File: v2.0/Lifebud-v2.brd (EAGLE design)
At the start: 100 x 80 mm, 47 parts, among them IC1 MCP73831/OT, Q1 BSS138, Q2 BSS138, Q3 BSS138, U2 MIC5219 3.3V, U3 MMA8452Q, U4 FT232RL, Y1 32.768kHz

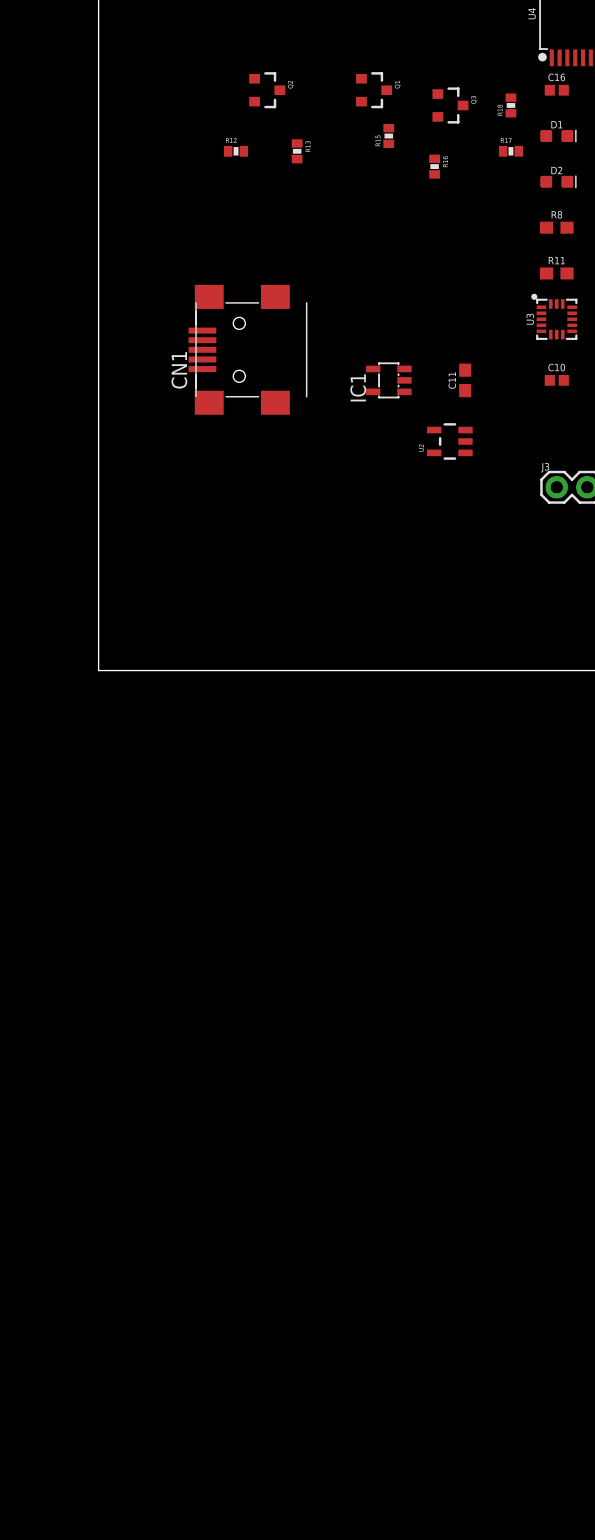
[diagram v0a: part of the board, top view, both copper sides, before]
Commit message: nearly finished with the DC/DC converter setup on nrf51
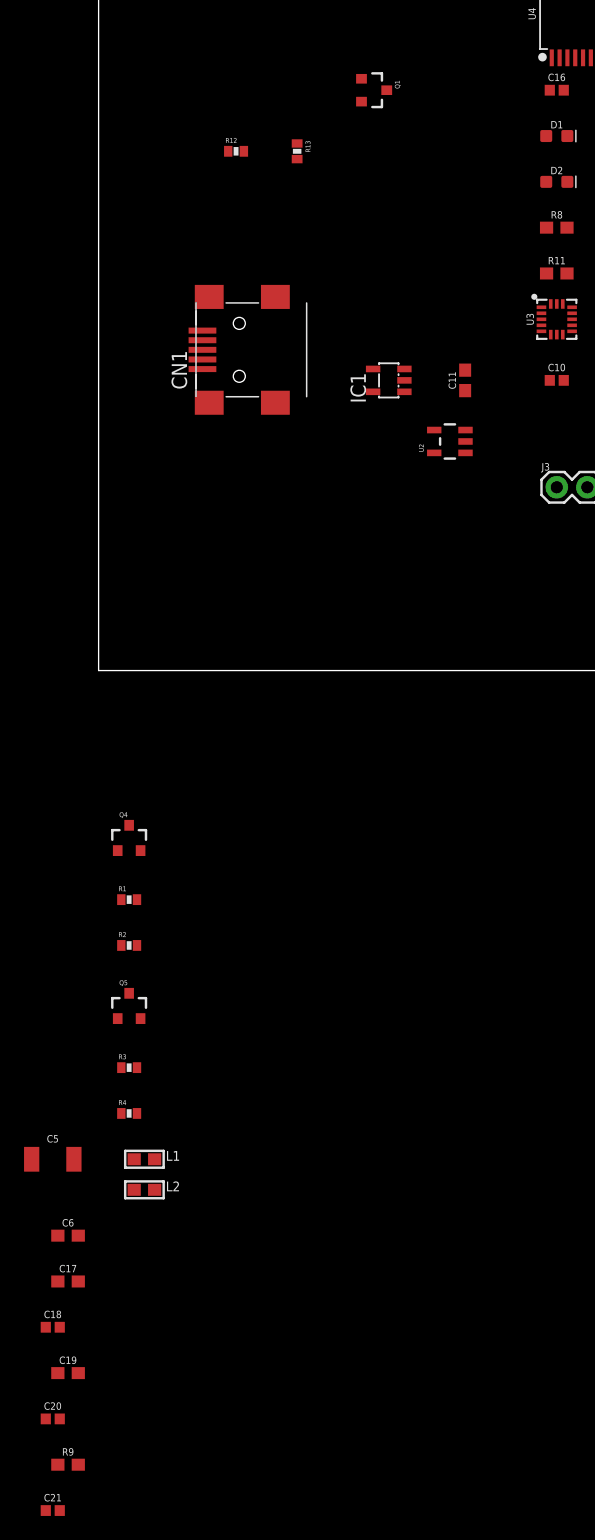
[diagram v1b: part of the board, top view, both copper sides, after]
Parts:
- removed Q2, Q3: BSS138, SparkFun:SOT23-3
- removed R15, R16, R17, R18: 10K, SparkFun:0402-RES
- added C17, C6: 1.0uF, SparkFun-Capacitors:0603
- added C18, C20, C21: 0.1uF, SparkFun-Capacitors:0402
- added C19: 4.7uF, SparkFun-Capacitors:0603
- added C5: 22UF, SparkFun-Capacitors:1210
- added L1: 10nH, microbuilder:0603
- added L2: 15nH, microbuilder:0603
- added Q4, Q5: BSS138, SparkFun:SOT23-3
- added R1, R2, R3, R4: 10K, SparkFun:0402-RES
- added R9: 10k, SparkFun-Resistors:0603
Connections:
- net N$17 renamed MAX_INT
- removed net N$18: J3.4
- removed net N$19: J3.3
- new net AVDD: C17.2, C6.1, L2.1
- new net MMA_I1: J3.4, U3.9
- new net MMA_I2: J3.3, U3.11
- new net N$20: L1.1, L2.2
- new net N$22: L1.2, U$2.15
- new net N$24: C18.2, U3.2
- new net N$25: R9.2, U3.7
- net +3V3: now also Q4.1, Q5.1, R1.1, R3.1; no longer Q2.1, Q3.1, R15.1, R17.1
- net 3V3: no longer U$1.A3
- net GND: now also C17.1, C18.1, C19.1, C20.1, C21.2, C5.1, C6.2, U3.10, U3.12, U3.5
- net INT_IN: now also Q5.3, R4.2; no longer Q3.3, R18.2
- net INT_OUT: now also Q5.2, R3.2; no longer Q3.2, R17.2
- net SCL_OUT: now also U3.4
- net SDA_IN: now also Q4.3, R2.2; no longer Q2.3, R16.2
- net SDA_OUT: now also Q4.2, R1.2, U3.6; no longer Q2.2, R15.2
- net VCC: now also C19.2, C20.2, C21.1, R2.1, R4.1, R9.1, U$1.A3, U3.1, U3.14; no longer R16.1, R18.1
- net VDD: now also C5.2

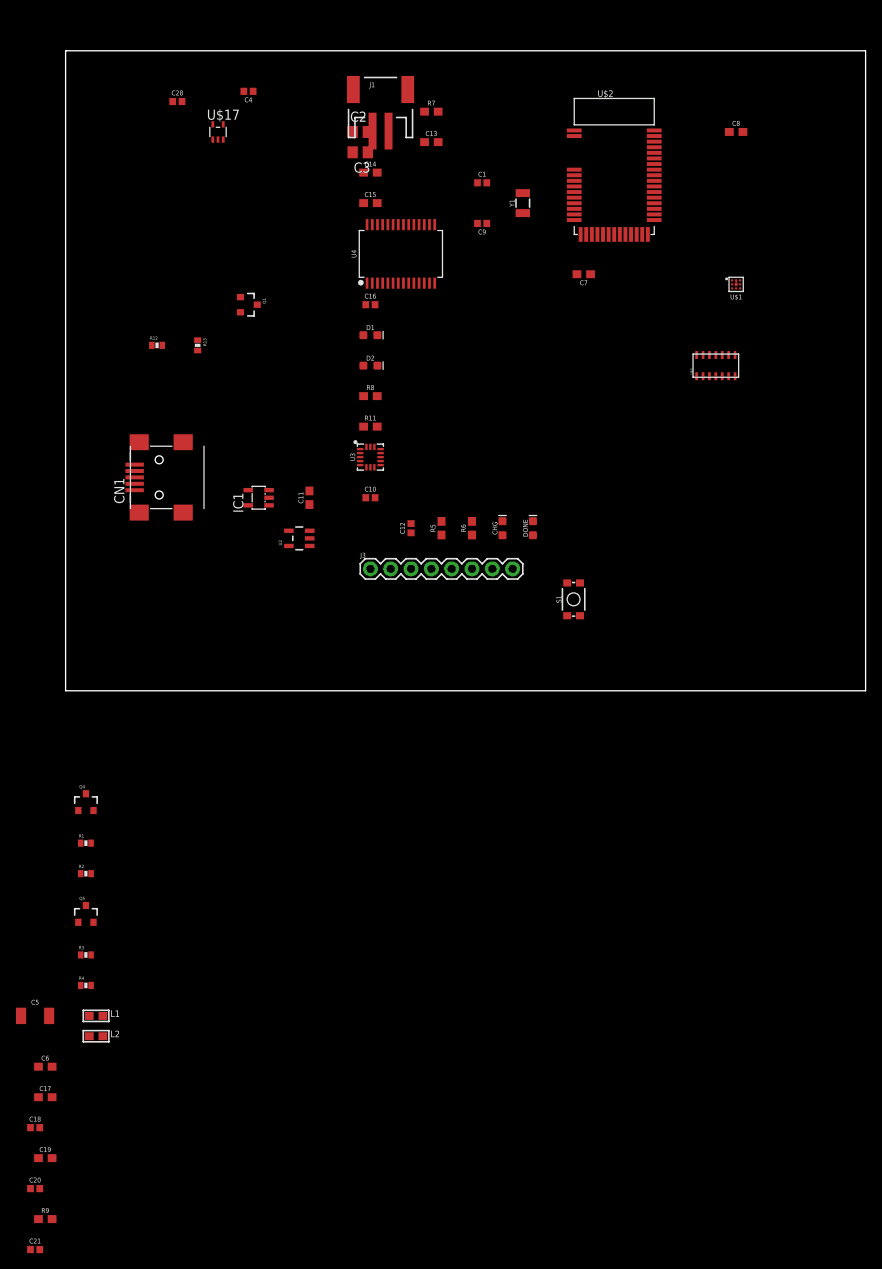
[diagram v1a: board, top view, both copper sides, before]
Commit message: cleaned up schematic, need to check for errors with ERC
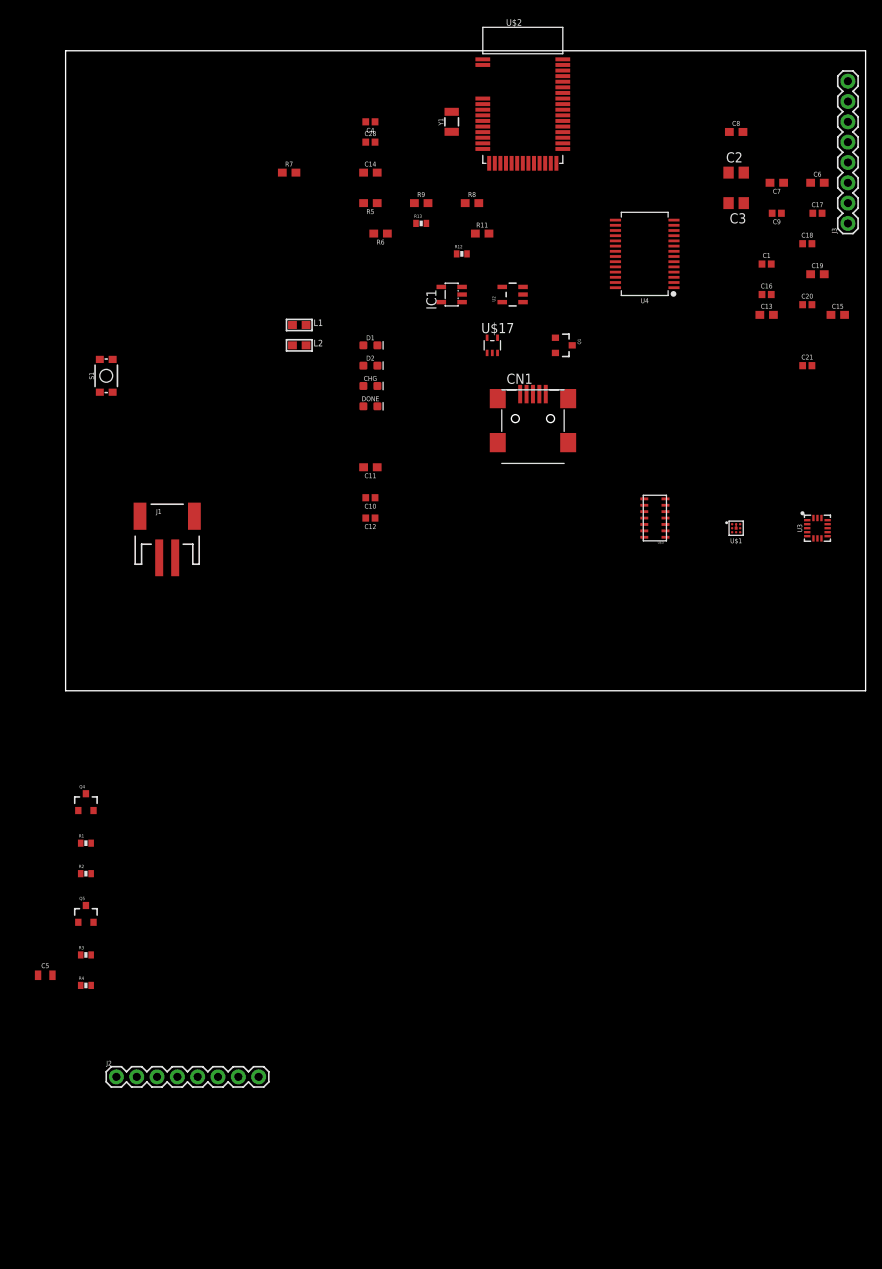
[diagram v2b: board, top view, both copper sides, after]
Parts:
- added J2: (no value), SparkFun-Connectors:1X08
- C17: value 1.0uF -> 100PF; device SparkFun-Capacitors:0603 -> SparkFun-Capacitors:0402
- C5: value 22UF -> 22uF; device SparkFun-Capacitors:1210 -> SparkFun-Capacitors:0805
- C7: value 1.0uF -> 1uF
- moved C17 146.7 mm to (94.0, 59.7)
- moved C18 146.7 mm to (92.7, 55.9)
- moved C19 146.7 mm to (94.0, 52.1)
- moved C20 146.7 mm to (92.7, 48.3)
- moved C21 146.7 mm to (92.7, 40.6)
- moved C6 146.7 mm to (94.0, 63.5)
- moved R9 135.4 mm to (44.5, 61.0)
- moved L1 90.0 mm to (29.2, 45.7)
- moved L2 90.0 mm to (29.2, 43.2)
- moved J3 73.7 mm to (97.8, 58.4), turned to 90 degrees
- moved S1 64.8 mm to (5.08, 39.4)
- moved C15 60.1 mm to (96.5, 47.0)
- moved J1 59.6 mm to (12.7, 20.3)
- moved U3 56.6 mm to (94.0, 20.3)
- moved C16 49.5 mm to (87.6, 49.5)
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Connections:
- net USBDM_IN renamed D-
- net USBDP_IN renamed D+
- removed net +3V3: Q1.1, Q4.1, Q5.1, R1.1, R12.1, R3.1
- removed net N$15: U$2.33
- removed net RXI: U$2.29, U4.5
- removed net TXO: U$2.27, U4.1
- removed net VCC: C10.2, C13.1, C19.2, C20.2, C21.1, C4.1, IC1.3, J1.2, R13.1, R2.1, R4.1, R9.1, U$1.A3, U$17.1, U$17.3, U$2.3, U2.1, U2.3, U3.1, U3.14, U4.20
- removed net VCCIO: C16.1, R11.2, R8.2, U4.17, U4.4
- removed net VDD: C5.2, C7.1, U$2.14
- removed net VUSB: C11.1, C12.1, CHG.A, CN1.VBUS, IC1.4
- new net 3V3OUT: C16.1, U4.17, U4.4
- new net N$23: J2.4
- new net N$26: J2.3
- new net N$27: J2.2
- new net N$28: J2.1
- new net RXD: J2.8, U$2.29, U4.5
- new net TXD: J2.6, U$2.27, U4.1
- new net VBAT: C13.1, C19.2, C20.2, C21.1, IC1.3, J1.2, R13.1, R2.1, R4.1, R9.1, U$1.A3, U2.1, U2.3, U3.1, U3.14
- new net VBUS: C11.1, C12.1, CHG.A, CN1.VBUS, IC1.4, U4.20
- net 3V3: now also C10.2, C4.1, C5.2, C7.2, Q1.1, Q4.1, Q5.1, R1.1, R11.2, R12.1, R3.1, R8.2, U$17.1, U$17.3, U$2.14, U$2.3
- net CTS: now also J2.7
- net GND: now also C1.2, C7.1; no longer C1.1, C7.2
- net N$4: now also C1.1; no longer C1.2
- net RTS: now also J2.5

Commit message: organized components using the line tool
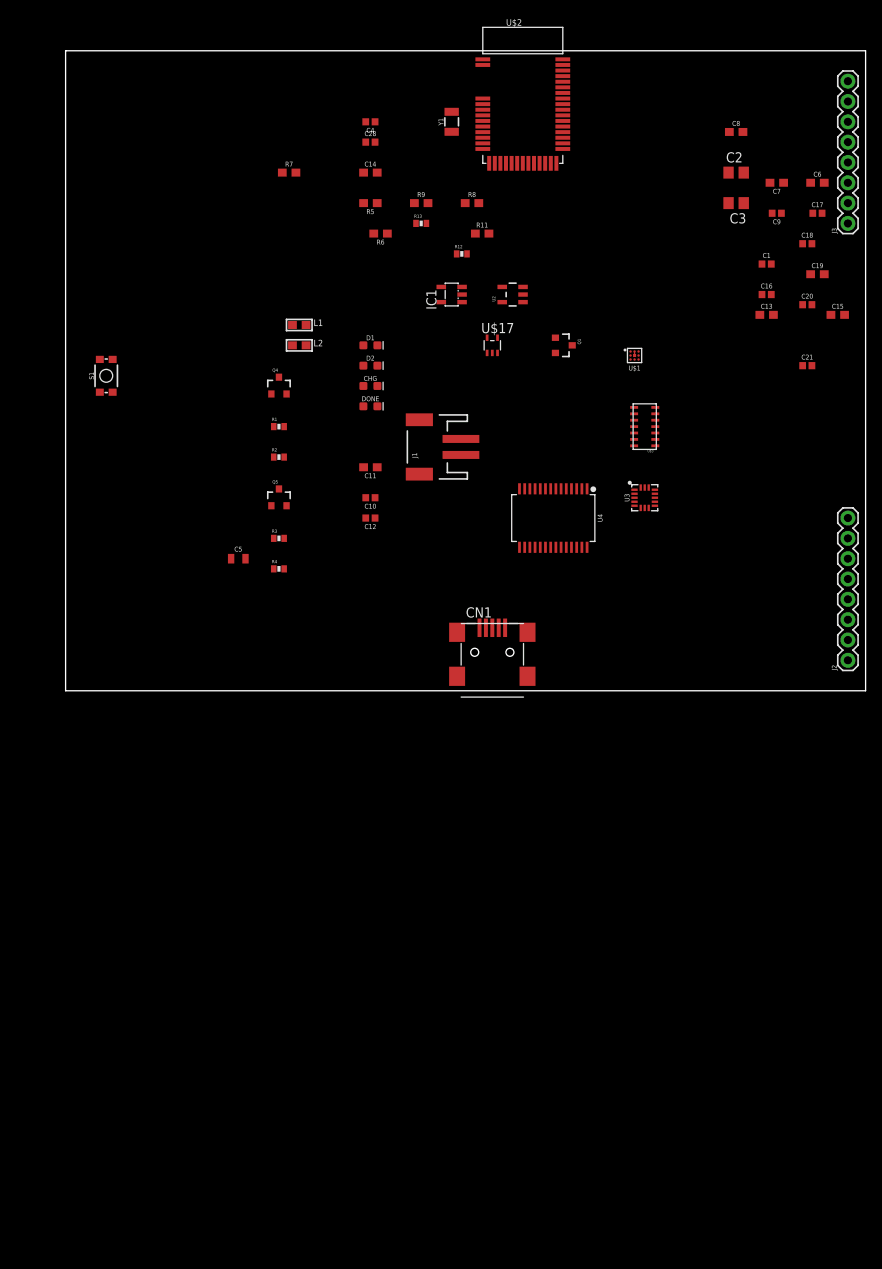
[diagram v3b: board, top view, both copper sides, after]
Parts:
- S1: value MOMENTARY-SWITCH-SPST-SMD-4.6X2.8MM -> MOMENTARY-SWITCH-SPST
- moved J2 105.2 mm to (97.8, 3.81), turned to 90 degrees
- moved C5 57.4 mm to (21.6, 16.5)
- moved R1 57.4 mm to (26.7, 33.0)
- moved R3 57.4 mm to (26.7, 19.1)
- moved Q4 57.4 mm to (26.7, 38.1)
- moved Q5 57.4 mm to (26.7, 24.1)
- moved R2 57.4 mm to (26.7, 29.2)
- moved R4 57.4 mm to (26.7, 15.2)
- moved U4 34.9 mm to (61.0, 21.6), turned to 180 degrees
- moved J1 34.5 mm to (45.7, 30.5), turned to 90 degrees
- moved CN1 29.6 mm to (53.3, 3.81)
- moved U$1 25.0 mm to (71.1, 41.9)
- moved U3 21.9 mm to (72.4, 24.1)
- moved U$3 11.5 mm to (72.4, 33.0)
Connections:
- new net VCC: C19.2, C20.2, C21.1, R13.1, R2.1, R4.1, R9.1, S1.3, S1.4, U$1.A3, U2.1, U2.3, U3.1, U3.14
- net VBAT: now also S1.1, S1.2; no longer C19.2, C20.2, C21.1, R13.1, R2.1, R4.1, R9.1, U$1.A3, U2.1, U2.3, U3.1, U3.14
